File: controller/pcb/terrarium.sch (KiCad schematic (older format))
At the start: 53 parts, among them K1 G3MB-202P, K2 G3MB-202P, K3 G3MB-202P, Q1 S8050, Q2 S8050, Q3 S8050, SW1 RST, U1 ESP32-WROOM-32, U2 DS3231M, U5 TCA9548APWR

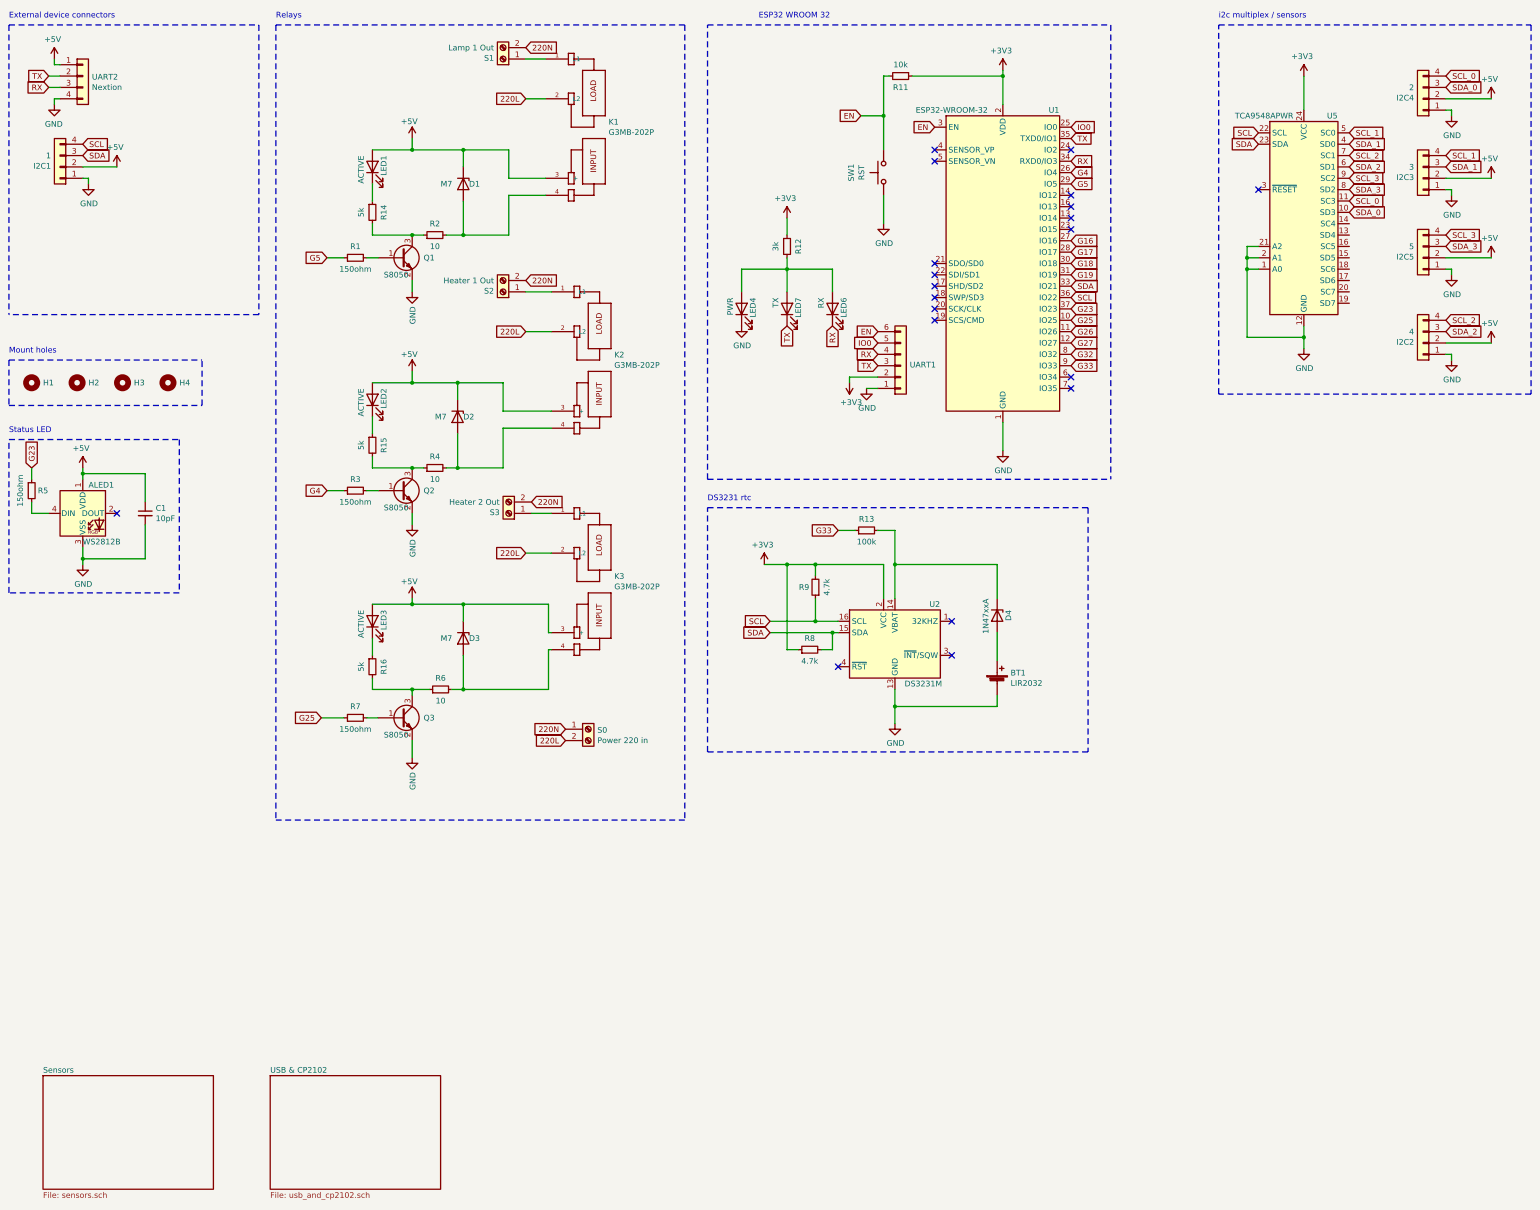
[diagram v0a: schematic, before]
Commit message: feat: add 5 pin sensor connectors
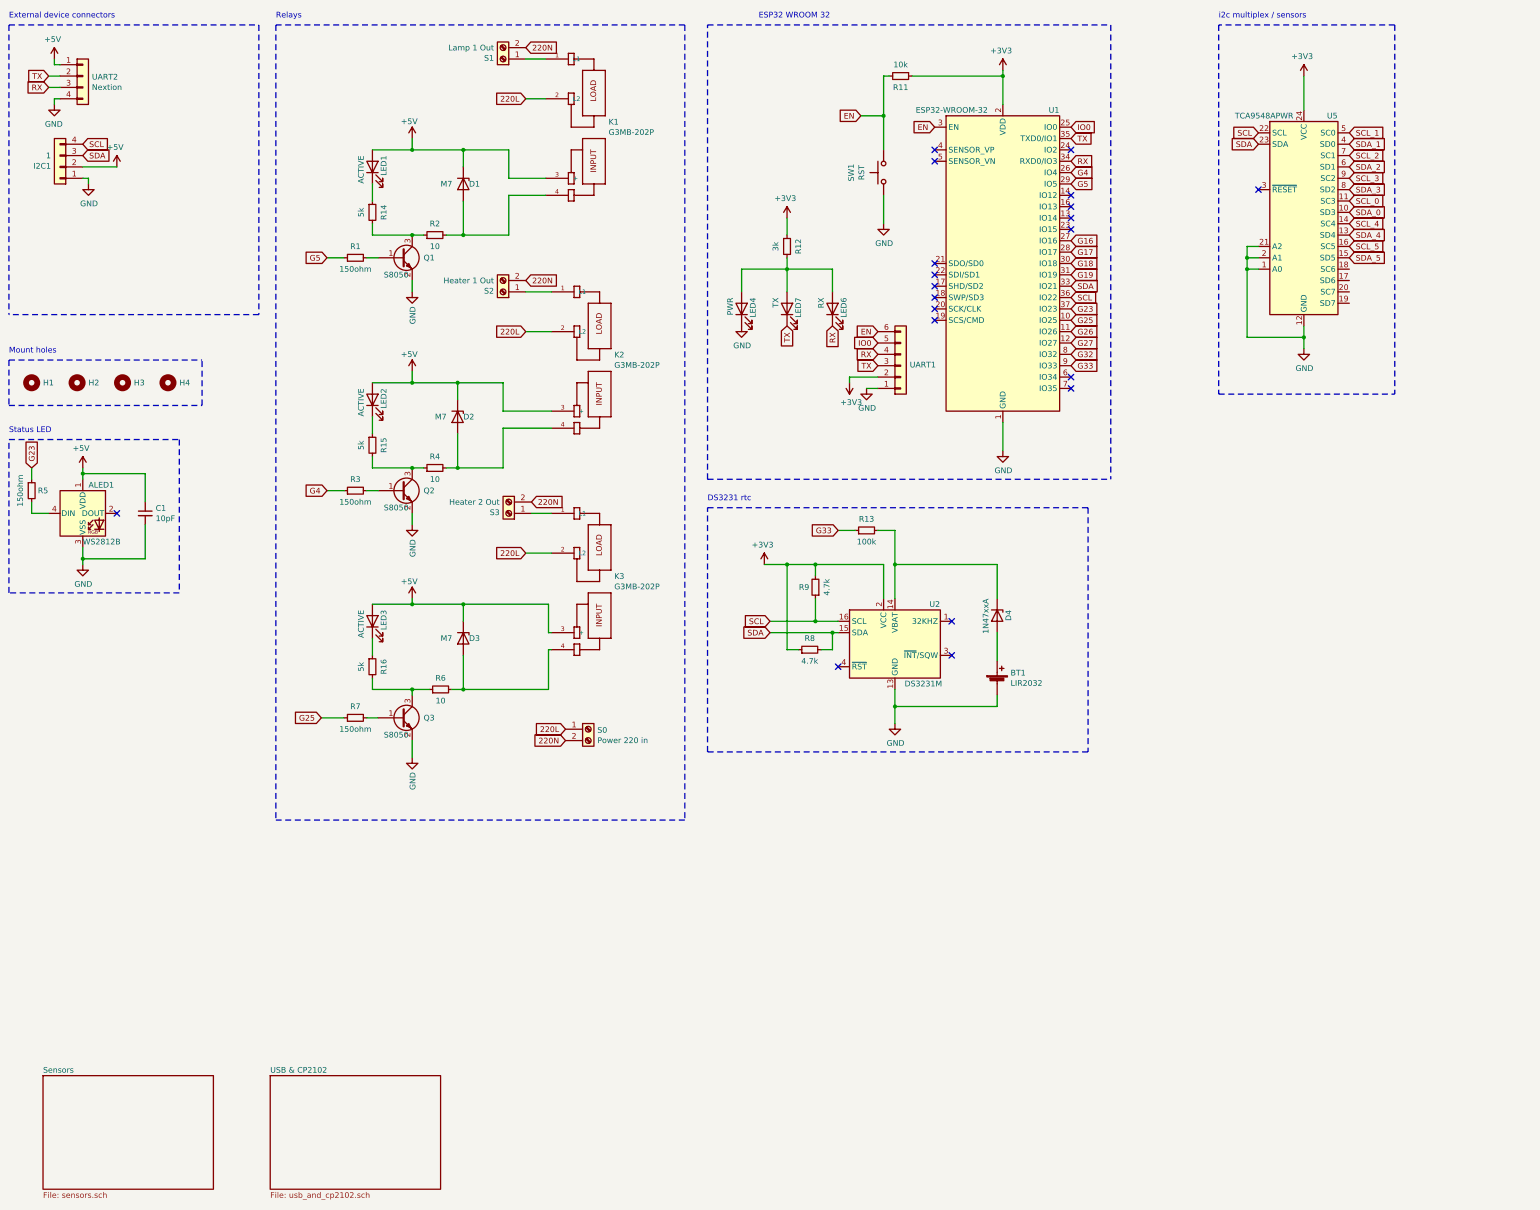
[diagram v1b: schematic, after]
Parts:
- removed I2C2: 4, Connector_JST:JST_XH_B4B-XH-AM_1x04_P2.50mm_Vertical, symbol Connector_Generic:Conn_01x04
- removed I2C3: 3, Connector_JST:JST_XH_B4B-XH-AM_1x04_P2.50mm_Vertical, symbol Connector_Generic:Conn_01x04
- removed I2C4: 2, Connector_JST:JST_XH_B4B-XH-AM_1x04_P2.50mm_Vertical, symbol Connector_Generic:Conn_01x04
- removed I2C5: 5, Connector_JST:JST_XH_B4B-XH-AM_1x04_P2.50mm_Vertical, symbol Connector_Generic:Conn_01x04
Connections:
- net 220L: now also S0.1 (Pin_1); no longer S0.2 (Pin_2)
- net 220N: now also S0.2 (Pin_2); no longer S0.1 (Pin_1)
- net SDA_4: now reaches U5.13 (SD4)
- net SCL_4: now reaches U5.14 (SC4)
- net SDA_5: now reaches U5.15 (SD5)
- net SCL_5: now reaches U5.16 (SC5)
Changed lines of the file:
@@
 	1    0    0    -1
 $EndComp
+Text GLabel 5600 7000 0    50   Input ~ 0
+220N
 Text GLabel 5600 6900 0    50   Input ~ 0
-220N
-Text GLabel 5600 7000 0    50   Input ~ 0
 220L
 Text GLabel 5250 3400 0    50   Input ~ 0
@@
 Wire Wire Line
 	1650 1950 1350 1950
-$Comp
-L Connector_Generic:Conn_01x04 I2C2
-U 1 1 6231B2F4
-P 13150 3500
-F 0 "I2C2" H 13230 3492 50  0000 L CNN
-F 1 "4" H 13230 3401 50  0000 L CNN
-F 2 "Connector_JST:JST_XH_B4B-XH-AM_1x04_P2.50mm_Vertical" H 13150 3500 50  0001 C CNN
-F 3 "~" H 13150 3500 50  0001 C CNN
-	1    13150 3500
-	-1   0    0    1
-$EndComp
-Text GLabel 13350 3300 2    50   Input ~ 0
-SCL_2
-Text GLabel 13350 3400 2    50   Input ~ 0
-SDA_2
-$Comp
-L power:GND #PWR014
-U 1 1 6231B2FC
-P 13400 3650
-F 0 "#PWR014" H 13400 3400 50  0001 C CNN
-F 1 "GND" H 13405 3477 50  0000 C CNN
-F 2 "" H 13400 3650 50  0001 C CNN
-F 3 "" H 13400 3650 50  0001 C CNN
-	1    13400 3650
-	1    0    0    -1
-$EndComp
-Wire Wire Line
-	13400 3650 13400 3600
-Wire Wire Line
-	13400 3600 13350 3600
-$Comp
-L power:+5V #PWR016
-U 1 1 6231B304
-P 13750 3500
-F 0 "#PWR016" H 13750 3350 50  0001 C CNN
-F 1 "+5V" H 13765 3673 50  0000 C CNN
-F 2 "" H 13750 3500 50  0001 C CNN
-F 3 "" H 13750 3500 50  0001 C CNN
-	1    13750 3500
-	-1   0    0    -1
-$EndComp
-$Comp
-L Connector_Generic:Conn_01x04 I2C5
-U 1 1 6232A2C4
-P 13150 2750
-F 0 "I2C5" H 13230 2742 50  0000 L CNN
-F 1 "5" H 13230 2651 50  0000 L CNN
-F 2 "Connector_JST:JST_XH_B4B-XH-AM_1x04_P2.50mm_Vertical" H 13150 2750 50  0001 C CNN
-F 3 "~" H 13150 2750 50  0001 C CNN
-	1    13150 2750
-	-1   0    0    1
-$EndComp
-Text GLabel 13350 2550 2    50   Input ~ 0
-SCL_3
-Text GLabel 13350 2650 2    50   Input ~ 0
-SDA_3
-$Comp
-L power:GND #PWR019
-U 1 1 6232A2CC
-P 13400 2900
-F 0 "#PWR019" H 13400 2650 50  0001 C CNN
-F 1 "GND" H 13405 2727 50  0000 C CNN
-F 2 "" H 13400 2900 50  0001 C CNN
-F 3 "" H 13400 2900 50  0001 C CNN
-	1    13400 2900
-	1    0    0    -1
-$EndComp
-Wire Wire Line
-	13400 2900 13400 2850
-Wire Wire Line
-	13400 2850 13350 2850
-$Comp
-L power:+5V #PWR022
-U 1 1 6232A2D4
-P 13750 2750
-F 0 "#PWR022" H 13750 2600 50  0001 C CNN
-F 1 "+5V" H 13765 2923 50  0000 C CNN
-F 2 "" H 13750 2750 50  0001 C CNN
-F 3 "" H 13750 2750 50  0001 C CNN
-	1    13750 2750
-	-1   0    0    -1
-$EndComp
-$Comp
-L Connector_Generic:Conn_01x04 I2C3
-U 1 1 6233CBD6
-P 13150 2050
-F 0 "I2C3" H 13230 2042 50  0000 L CNN
-F 1 "3" H 13230 1951 50  0000 L CNN
-F 2 "Connector_JST:JST_XH_B4B-XH-AM_1x04_P2.50mm_Vertical" H 13150 2050 50  0001 C CNN
-F 3 "~" H 13150 2050 50  0001 C CNN
-	1    13150 2050
-	-1   0    0    1
-$EndComp
-Text GLabel 13350 1850 2    50   Input ~ 0
-SCL_1
-Text GLabel 13350 1950 2    50   Input ~ 0
-SDA_1
-$Comp
-L power:GND #PWR017
-U 1 1 6233CBDE
-P 13400 2200
-F 0 "#PWR017" H 13400 1950 50  0001 C CNN
-F 1 "GND" H 13405 2027 50  0000 C CNN
-F 2 "" H 13400 2200 50  0001 C CNN
-F 3 "" H 13400 2200 50  0001 C CNN
-	1    13400 2200
-	1    0    0    -1
-$EndComp
-Wire Wire Line
-	13400 2200 13400 2150
-Wire Wire Line
-	13400 2150 13350 2150
-$Comp
-L power:+5V #PWR020
-U 1 1 6233CBE6
-P 13750 2050
-F 0 "#PWR020" H 13750 1900 50  0001 C CNN
-F 1 "+5V" H 13765 2223 50  0000 C CNN
-F 2 "" H 13750 2050 50  0001 C CNN
-F 3 "" H 13750 2050 50  0001 C CNN
-	1    13750 2050
-	-1   0    0    -1
-$EndComp
 Wire Notes Line
 	2900 3250 700  3250
@@
 Text GLabel 12500 1850 2    50   Input ~ 0
 SCL_2
-$Comp
-L power:+5V #PWR021
-U 1 1 6230B24A
-P 13750 1350
-F 0 "#PWR021" H 13750 1200 50  0001 C CNN
-F 1 "+5V" H 13765 1523 50  0000 C CNN
-F 2 "" H 13750 1350 50  0001 C CNN
-F 3 "" H 13750 1350 50  0001 C CNN
-	1    13750 1350
-	-1   0    0    -1
-$EndComp
-Wire Wire Line
-	13400 1450 13350 1450
-Wire Wire Line
-	13400 1500 13400 1450
-$Comp
-L power:GND #PWR018
-U 1 1 6230B242
-P 13400 1500
-F 0 "#PWR018" H 13400 1250 50  0001 C CNN
-F 1 "GND" H 13405 1327 50  0000 C CNN
-F 2 "" H 13400 1500 50  0001 C CNN
-F 3 "" H 13400 1500 50  0001 C CNN
-	1    13400 1500
-	1    0    0    -1
-$EndComp
-Text GLabel 13350 1250 2    50   Input ~ 0
-SDA_0
-Text GLabel 13350 1150 2    50   Input ~ 0
-SCL_0
-$Comp
-L Connector_Generic:Conn_01x04 I2C4
-U 1 1 6230B23A
-P 13150 1350
-F 0 "I2C4" H 13230 1342 50  0000 L CNN
-F 1 "2" H 13230 1251 50  0000 L CNN
-F 2 "Connector_JST:JST_XH_B4B-XH-AM_1x04_P2.50mm_Vertical" H 13150 1350 50  0001 C CNN
-F 3 "~" H 13150 1350 50  0001 C CNN
-	1    13150 1350
-	-1   0    0    1
-$EndComp
-Wire Wire Line
-	13350 1350 13750 1350
-Wire Wire Line
-	13350 2050 13750 2050
-Wire Wire Line
-	13350 3500 13750 3500
-Wire Wire Line
-	13350 2750 13750 2750
-Wire Notes Line
-	11350 700  14100 700
-Wire Notes Line
-	14100 700  14100 3950
-Wire Notes Line
-	14100 3950 11350 3950
-Wire Notes Line
-	11350 3950 11350 700
 Text Notes 11350 650  0    50   ~ 0
 i2c multiplex / sensors
+Text GLabel 12500 2550 2    50   Input ~ 0
+SDA_4
+Text GLabel 12500 2750 2    50   Input ~ 0
+SDA_5
+Text GLabel 12500 2450 2    50   Input ~ 0
+SCL_4
+Text GLabel 12500 2650 2    50   Input ~ 0
+SCL_5
+Wire Notes Line
+	12900 700  12900 3950
+Wire Notes Line
+	12900 700  11350 700
+Wire Notes Line
+	11350 700  11350 3950
+Wire Notes Line
+	11350 3950 12900 3950
 $EndSCHEMATC

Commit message: rearrange components
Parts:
- added PWR1: data, Connector_PinHeader_2.54mm:PinHeader_1x01_P2.54mm_Vertical, symbol Connector_Generic:Conn_01x01
- I2C1: value 1 -> LCD
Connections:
- net +5V: now also PWR1.1 (Pin_1)
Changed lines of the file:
@@
 P 1150 1950
 F 0 "I2C1" H 1230 1942 50  0000 L CNN
-F 1 "1" H 1230 1851 50  0000 L CNN
+F 1 "LCD" H 1230 1851 50  0000 L CNN
 F 2 "Connector_JST:JST_XH_B4B-XH-AM_1x04_P2.50mm_Vertical" H 1150 1950 50  0001 C CNN
 F 3 "~" H 1150 1950 50  0001 C CNN
@@
 Wire Notes Line
 	11350 3950 12900 3950
+$Comp
+L Connector_Generic:Conn_01x01 PWR1
+U 1 1 62095041
+P 7150 4150
+F 0 "PWR1" H 7230 4142 50  0000 L CNN
+F 1 "data" H 7300 3550 50  0001 L CNN
+F 2 "Connector_PinHeader_2.54mm:PinHeader_1x01_P2.54mm_Vertical" H 7150 4150 50  0001 C CNN
+F 3 "~" H 7150 4150 50  0001 C CNN
+	1    7150 4150
+	0    -1   1    0
+$EndComp
+$Comp
+L power:+5V #PWR014
+U 1 1 6209A4E1
+P 7150 3950
+F 0 "#PWR014" H 7150 3800 50  0001 C CNN
+F 1 "+5V" H 7050 4100 50  0000 L CNN
+F 2 "" H 7150 3950 50  0001 C CNN
+F 3 "" H 7150 3950 50  0001 C CNN
+	1    7150 3950
+	1    0    0    -1
+$EndComp
 $EndSCHEMATC

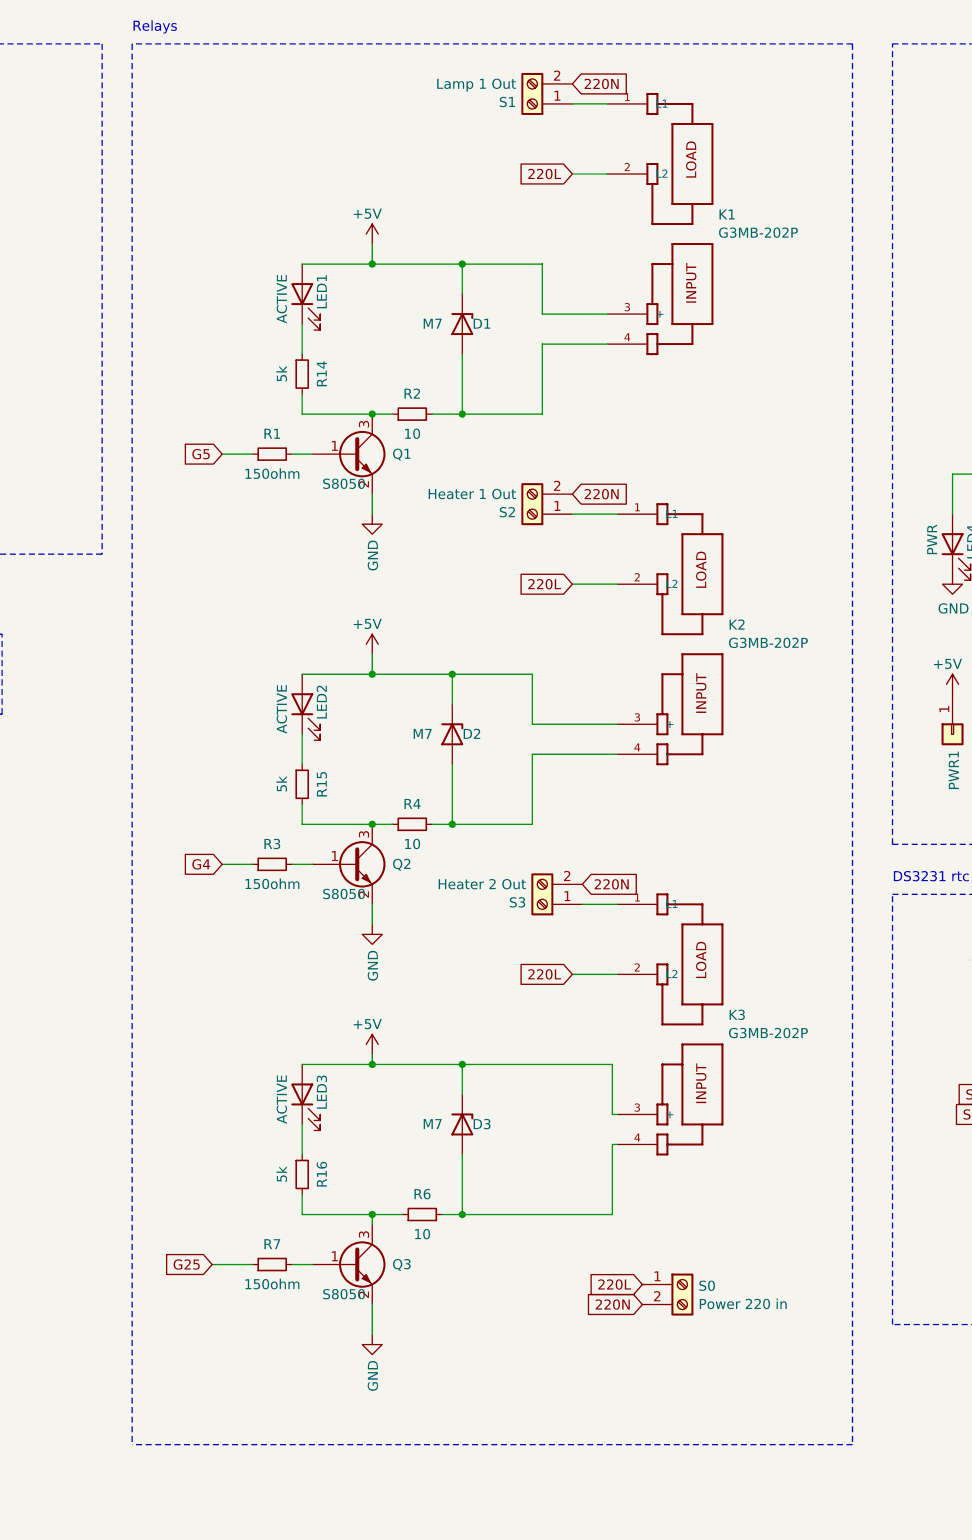
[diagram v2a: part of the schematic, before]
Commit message: update ssr circuits
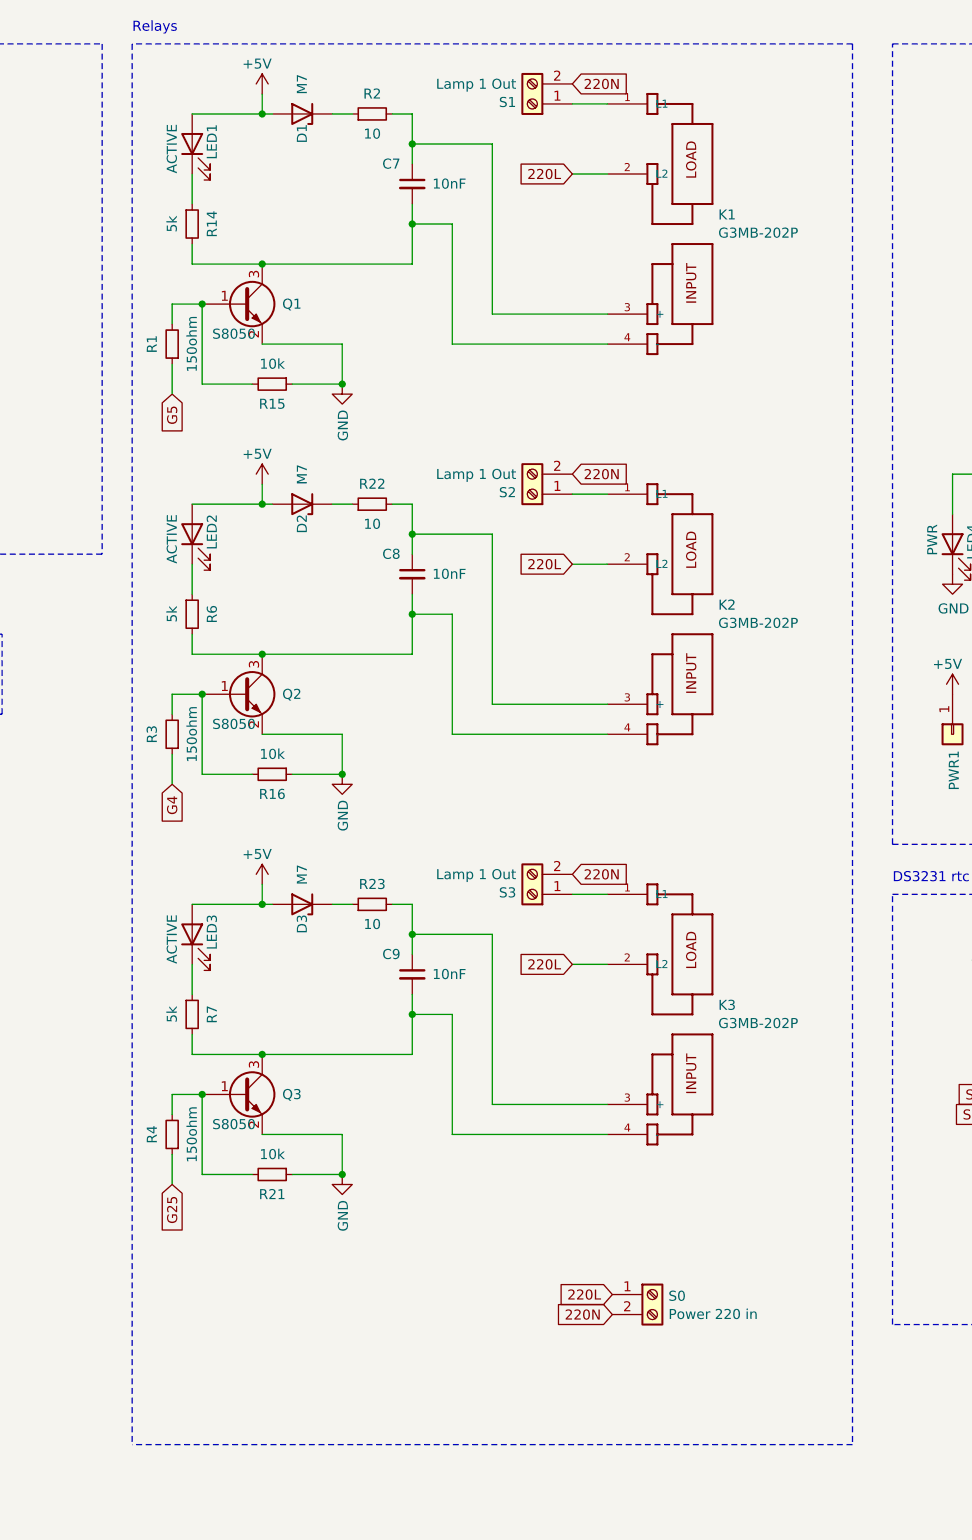
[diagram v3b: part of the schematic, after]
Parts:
- added C7, C8, C9: 10nF, Capacitor_SMD:C_1206_3216Metric, symbol Device:C_Small
- added R21: 10k, Resistor_SMD:R_1206_3216Metric, symbol Device:R_Small
- added R22, R23: 10, Resistor_SMD:R_1206_3216Metric, symbol Device:R_Small
- K1, K2, K3: footprint Omron:RELAY_G3MB-202P -> omron:RELAY_G3MB-202P
- R15, R16: value 5k -> 10k
- R4: value 10 -> 150ohm
- R6: value 10 -> 5k
- R7: value 150ohm -> 5k
- S2: value Heater 1 Out -> Lamp 1 Out
- S3: value Heater 2 Out -> Lamp 1 Out
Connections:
- net +5V: now also D1.2 (A), D2.2 (A), D3.2 (A); no longer D1.1 (K), D2.1 (K), D3.1 (K), K1.3 (+), K2.3 (+), K3.3 (+)
- net G25: now also R4.1; no longer R7.1
- net GND: now also R15.1, R16.1, R21.1
- net at Q1.3 (C), R14.2: now also K1.4 (-), C7.2; no longer R2.1
- net at Q1.1 (B), R1.2: now also R15.2
- net at Q2.1 (B), R3.2: now also R16.2
- net at LED2.1 (K): now also R6.1; no longer R15.1
- net at Q3.1 (B): now also R4.2, R21.2; no longer R7.2
- net at LED3.1 (K): now also R7.1; no longer R16.1
- new net: D1.1 (K), R2.1
- new net: C7.1, K1.3 (+), R2.2
- new net: C8.1, K2.3 (+), R22.2
- new net: C8.2, K2.4 (-), Q2.3 (C), R6.2
- new net: D2.1 (K), R22.1
- new net: C9.1, K3.3 (+), R23.2
- new net: C9.2, K3.4 (-), Q3.3 (C), R7.2
- new net: D3.1 (K), R23.1
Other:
- moved on the sheet: D1, LED1, Q1, R1, R14, R2, S0
